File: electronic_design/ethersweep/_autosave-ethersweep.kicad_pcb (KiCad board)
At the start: 2 copper layers, 79 x 38 mm, 101 parts, among them J1 AVR-ISP-6, J10 HR911105A, J11 Conn_01x04_Male, J2 Conn_01x02_Male, J3 Conn_01x04_Female, J4 Conn_01x02_Male, J5 Conn_01x02_Male, J6 Conn_01x07_Female, J7 Conn_01x07_Male, J8 AVR-ISP-6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

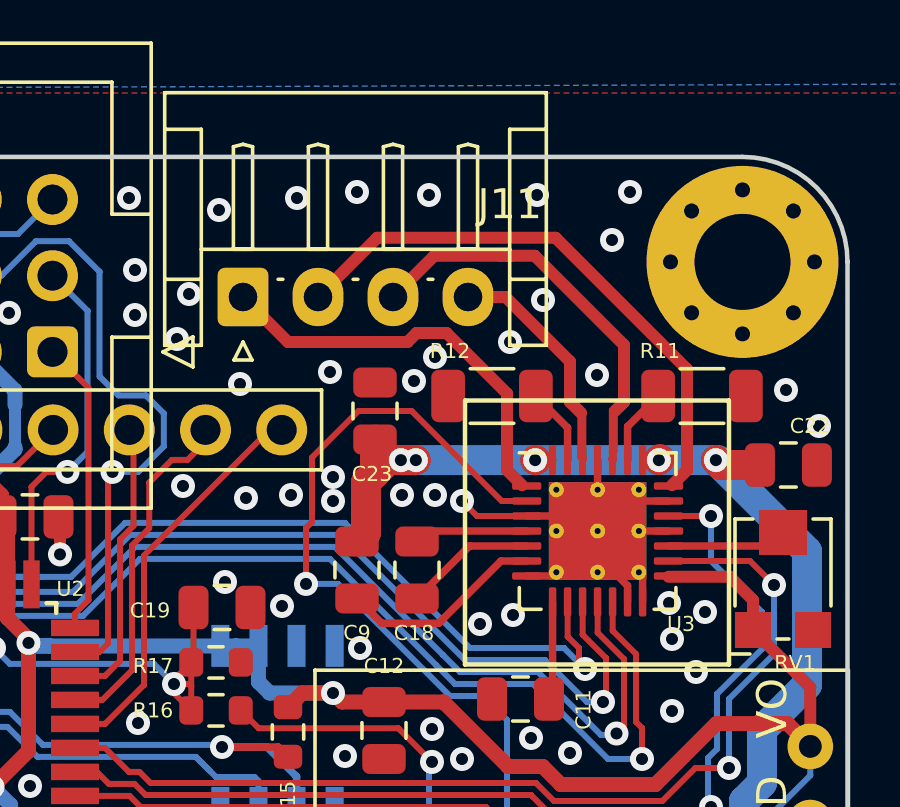
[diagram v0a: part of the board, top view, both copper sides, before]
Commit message: changed pinout for nema17 motor to be parallel to connector
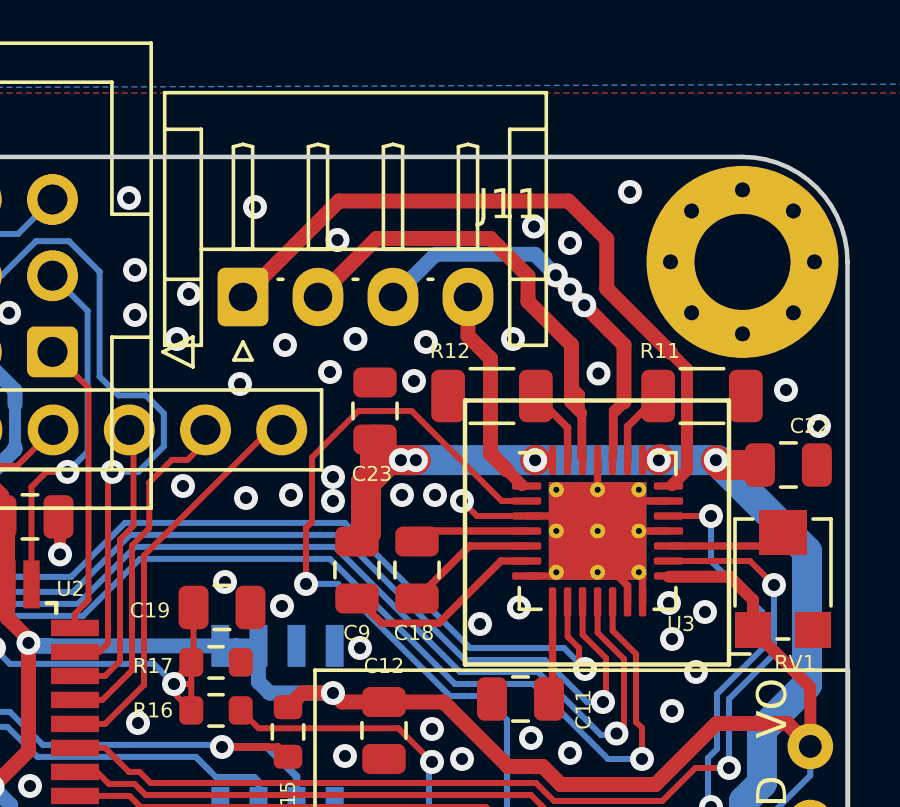
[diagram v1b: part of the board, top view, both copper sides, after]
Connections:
- U3 pad 1: Net-(J11-Pad1) -> Net-(J11-Pad4)
- U3 pad 21: Net-(J11-Pad2) -> Net-(J11-Pad1)
- U3 pad 26: Net-(J11-Pad4) -> Net-(J11-Pad2)
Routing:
- net Net-(J11-Pad1): track 13.6 -> 23.5 mm
- net Net-(J11-Pad4): track 10.3 -> 7.02 mm
- net Net-(J11-Pad3): track 15.5 -> 17.6 mm, vias 0 -> 3
- net Net-(J11-Pad2): track 19.0 -> 19.6 mm
- net GND: vias 227 -> 226
